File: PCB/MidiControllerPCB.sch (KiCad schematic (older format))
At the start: 148 parts, among them J1 BARREL_JACK, J10 L10_Out, J11 L9_In, J12 L9_Out, J13 4_In, J14 4_Out, J15 3_In, J16 3_Out, J17 2_In, J18 2_Out, J19 1_In, J2 LMain_Out, J20 1_Out, J21 DIN_5, J22 Vol_In, J23 Vol_Out, J24 Tap1, J25 Tap2, J26 ToMainOutL, J27 MainOutL, J28 ToVolInOut, J29 VolInOut, J3 Tap3, J35 Raspberry_Pi_2_3, J4 Tap4, J41 PIC_debug, J44 pi 1=pwr 2=gnd, J5 LEDs / LCD / FootSwitches, J6 Pedal Routes, J7 DIN_5, J8 DIN_5, J9 L10_In, K1 AZ850-x, K10 AZ850-x, K11 AZ850-x, K12 AZ850-x, K13 AZ850-x, K14 AZ850-x, K15 AZ850-x, K16 AZ850-x, K17 AZ850-x, K2 AZ850-x, K3 AZ850-x, K4 AZ850-x, K5 AZ850-x, K6 AZ850-x, K7 AZ850-x, K8 AZ850-x, K9 AZ850-x, Q1 Q_NPN_BEC, Q10 Q_NPN_BEC, Q11 Q_NPN_BEC, Q12 Q_NPN_BEC, Q13 Q_NPN_BEC, Q14 Q_NPN_BEC, Q15 Q_NPN_BEC, Q16 Q_NPN_BEC, Q17 Q_NPN_BEC, Q18 Q_NPN_BEC, Q19 Q_NPN_BEC, Q2 Q_NPN_BEC, Q20 Q_NPN_BEC, Q21 Q_NPN_BEC, Q22 Q_NPN_BEC, Q3 Q_NPN_BEC, Q4 Q_NPN_BEC, Q5 Q_NPN_BEC, Q6 Q_NPN_BEC, Q7 Q_NPN_BEC, Q8 Q_NPN_BEC, Q9 Q_NPN_BEC, U1 MCP23017_ML, U10 PIC18F26K80_IML, U2 MCP23017_ML, U3 MCP23017_ML, U4 MCP23017_ML, U5 CD4050BCN, U6 4N35, U7 7805_PINS, U8 TL072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

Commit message: progress toward schematic being done
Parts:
- removed C15, C17: 10uf, Capacitors_THT:CP_Radial_D4.0mm_P2.00mm, symbol Device:CP1_Small
- removed C16, C18: 0.1uf, Capacitors_THT:C_Axial_L3.8mm_D2.6mm_P7.50mm_Horizontal, symbol Device:C_Small
- removed D1, D10, D11, D12, D13, D14, D15, D17, D2, D20, D22, D3, D4, D5, D6, D7, D8, D9: 1N4001, Diodes_SMD:D_SMA, symbol MidiControllerPCB-rescue:1N4001-LooperPCB-rescue
- removed J1: BARREL_JACK, Connectors:BARREL_JACK, symbol conn:BARREL_JACK
- removed J10: L10_Out, NRJ6HM:NRJ6HM-1-PRE, symbol conn:JACK_TRS_6PINS
- removed J11: L9_In, NRJ6HM:NRJ6HM-1-PRE, symbol conn:JACK_TRS_6PINS
- removed J12: L9_Out, NRJ6HM:NRJ6HM-1-PRE, symbol conn:JACK_TRS_6PINS
- removed J13: 4_In, NRJ6HM:NRJ6HM-1-PRE, symbol conn:JACK_TRS_6PINS
- removed J14: 4_Out, NRJ6HM:NRJ6HM-1-PRE, symbol conn:JACK_TRS_6PINS
- removed J15: 3_In, NRJ6HM:NRJ6HM-1-PRE, symbol conn:JACK_TRS_6PINS
- removed J16: 3_Out, NRJ6HM:NRJ6HM-1-PRE, symbol conn:JACK_TRS_6PINS
- removed J17: 2_In, NRJ6HM:NRJ6HM-1-PRE, symbol conn:JACK_TRS_6PINS
- removed J18: 2_Out, NRJ6HM:NRJ6HM-1-PRE, symbol conn:JACK_TRS_6PINS
- removed J19: 1_In, NRJ6HM:NRJ6HM-1-PRE, symbol conn:JACK_TRS_6PINS
- removed J2: LMain_Out, NRJ6HM:NRJ6HM-1-PRE, symbol conn:JACK_TRS_6PINS
- removed J20: 1_Out, NRJ6HM:NRJ6HM-1-PRE, symbol conn:JACK_TRS_6PINS
- removed J21: DIN_5, stomp:Midi-Connector, symbol conn:DIN_5
- removed J22: Vol_In, NRJ6HM:NRJ6HM-1-PRE, symbol conn:JACK_TRS_6PINS
- removed J23: Vol_Out, NRJ6HM:NRJ6HM-1-PRE, symbol conn:JACK_TRS_6PINS
- removed J26: ToMainOutL, Pin_Headers:Pin_Header_Straight_2x05_Pitch2.54mm, symbol conn:CONN_02X05
- removed J27: MainOutL, Pin_Headers:Pin_Header_Straight_2x05_Pitch2.54mm, symbol conn:CONN_02X05
- removed J28: ToVolInOut, Pin_Headers:Pin_Header_Straight_2x05_Pitch2.54mm, symbol conn:CONN_02X05
- removed J29: VolInOut, Pin_Headers:Pin_Header_Straight_2x05_Pitch2.54mm, symbol conn:CONN_02X05
- removed J44: pi 1=pwr 2=gnd, Pin_Headers:Pin_Header_Straight_1x02_Pitch2.54mm, symbol conn:CONN_01X02
- removed J5: LEDs / LCD / FootSwitches, Pin_Headers:Pin_Header_Straight_2x20_Pitch2.54mm, symbol conn:CONN_02X20
- removed J6: Pedal Routes, Pin_Headers:Pin_Header_Straight_2x20_Pitch2.54mm, symbol conn:CONN_02X20
- removed J9: L10_In, NRJ6HM:NRJ6HM-1-PRE, symbol conn:JACK_TRS_6PINS
- removed K1, K10, K11, K12, K13, K14, K15, K16, K17, K2, K3, K4, K5, K6, K7, K8, K9: AZ850-x, Relays_THT:Relay_DPDT_FRT5, symbol MidiControllerPCB-rescue:AZ850-x-LooperPCB-rescue
- removed Q1, Q10, Q11, Q12, Q13, Q14, Q15, Q16, Q17, Q18, Q19, Q2, Q20, Q21, Q22, Q3, Q4, Q5, Q6, Q7, Q8, Q9: Q_NPN_BEC, TO_SOT_Packages_SMD:SOT-23, symbol Device:Q_NPN_BEC
- removed R1, R10, R11, R12, R13, R14, R2, R3, R30, R34, R4, R45, R5, R6, R7, R8, R9: 100, Resistors_SMD:R_1206_HandSoldering, symbol Device:R_Small
- removed R19, R57, R59, R61, R64: 470, Resistors_SMD:R_1206_HandSoldering, symbol Device:R_Small
- removed R20: 270, Resistors_SMD:R_1206_HandSoldering, symbol Device:R_Small
- removed R43: 1k, Resistors_SMD:R_1206_HandSoldering, symbol Device:R_Small
- removed R58, R60, R62, R65: 4.7k, Resistors_SMD:R_1206_HandSoldering, symbol Device:R_Small
- removed R75, R76, R77, R78, R79: 2.2M, Resistors_SMD:R_0603_HandSoldering, symbol Device:R_Small
- removed TP1: 9V, Pin_Headers:Pin_Header_Straight_1x01_Pitch2.54mm, symbol MidiControllerPCB-rescue:TEST-LooperPCB-rescue
- removed TP2: GND, Pin_Headers:Pin_Header_Straight_1x01_Pitch2.54mm, symbol MidiControllerPCB-rescue:TEST-LooperPCB-rescue
- removed U1, U3, U4: MCP23017_ML, Housings_DFN_QFN:QFN-28-1EP_6x6mm_Pitch0.65mm, symbol Interface_Expansion:MCP23017_ML
- removed U6: 4N35, Housings_DIP:DIP-6_W7.62mm_Socket, symbol 4N35-TTL-Serial-Optoisolator-cache:4N35
- removed U7: 7805_PINS, TO_SOT_Packages_THT:TO-220-3_Vertical, symbol eurocad:7805_PINS
- removed U8, U9: TL072, Housings_SSOP:TSSOP-8_4.4x3mm_Pitch0.65mm, symbol linear:TL072
- added C? (x5): 0.1uf, Capacitors_THT:C_Axial_L3.8mm_D2.6mm_P7.50mm_Horizontal, symbol Device:C_Small
- added C? (x2): 0.01uf, Capacitors_THT:C_Axial_L3.8mm_D2.6mm_P7.50mm_Horizontal, symbol Device:C_Small
- added J?: fan_header, symbol conn:CONN_01X02
- added J?: OLED_Display, symbol conn:CONN_01X07
- added R? (x15): 10k, Resistors_THT:R_Box_L8.4mm_W2.5mm_P5.08mm, symbol Device:R_Small
- added R? (x3): 1k, Resistors_THT:R_Box_L8.4mm_W2.5mm_P5.08mm, symbol Device:R_Small
- added R? (x8): 220, Resistors_SMD:R_1206_HandSoldering, symbol Device:R_Small
- added SW? (x5): SW_SPST, Pin_Headers:Pin_Header_Straight_1x02_Pitch2.54mm, symbol LooperPCB_side-rescue:SW_SPST
- added SW?: RGB_Rotary_Enc_PB, stomp:RGB_ENCODER_8pins, symbol LooperPCB_side-rescue:RGB_Rotary_Enc_PB
- J24: value Tap1 -> TRS_Midi_1
- J25: value Tap2 -> TRS_Midi_2
- J3: value Tap3 -> TRS_Midi_3
- J4: value Tap4 -> TRS_Midi_4
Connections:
- net FootSw6 is gone; now on net FootSw4: U2.25 (GPB0)
- net FootSw8 is gone; now on net FootSw5: U2.27 (GPB2)
- net 1_MIDI_Pin5: now also R18.1, U5.2 (G=A); no longer U5.4 (H=B)
- net 2_MIDI_Pin5: now also R16.1, U5.4 (H=B); no longer U5.2 (G=A)
- net FootSw1: now also C?.1, R?.1
- net FootSw2: now also C?.1, R?.1
- net FootSw3: now also C?.1, R?.1
- net FootSw4: now also C?.1, R?.1; no longer U2.20 (GPA3)
- net FootSw5: now also C?.1, R?.1; no longer U2.21 (GPA4)
- net GND: now also C?.2, C?.2, C?.2, C?.2, C?.2, C?.2, C?.2, J?.1 (P1), J?.2 (P2), R?.2, SW?.1 (A), SW?.1 (A), SW?.1 (A), SW?.1 (A), SW?.1 (A), SW?.2 (C)
- net MIDI_Tx: now also U5.11 (E), U5.14 (F), U5.7 (C), U5.9 (D)
- net RotEncA: now also C?.1, R?.2
- net RotEncB: now also C?.1, R?.1
- net RotEncBlue: now also R?.2
- net RotEncGreen: now also R?.2
- net RotEncPushBttn: now also R?.1, SW?.6 (SW)
- net RotEncRed: now also R?.2
- net VCC: now also J35.2 (5V), J?.1 (P1), R?.1, R?.1, R?.1, R?.1, R?.1, R?.1, R?.2, R?.2, R?.2, R?.2, R?.2, SW?.8 (+)
- net VEE: now also J?.2 (P2)
- net MOSI: now reaches J35.19 ((SPI_MOSI)_GPIO10)
- net MOSI: now also J?.5 (P5)
- net Reset: now reaches J35.22 (GPIO25_(GEN6))
- net Reset: now also J?.7 (P7)
- net SCLK: now reaches J35.23 ((SPI_SCLK)_GPIO11)
- net SCLK: now also J?.4 (P4)
- net ChipSelectEnable: now reaches J35.26 ((~SPI_CE1~)_GPIO7)
- net ChipSelectEnable: now also J?.6 (P6)
- net DataCommand: now reaches J35.32 (GPIO12)
- net DataCommand: now also J?.3 (P3)
- net at J3.2 (T): now also R?.2
- net at J4.2 (T): now also R?.2
- net at J24.2 (T): now also R?.2
- net at J25.2 (T): now also R?.2
- net 2_TRS_MIDI_Tip: now reaches U5.10 (J=D)
- net 2_TRS_MIDI_Tip: now also R?.1
- net 3_TRS_MIDI_Tip: now reaches U5.12 (K=E)
- net 3_TRS_MIDI_Tip: now also R?.1
- net 4_TRS_MIDI_Tip: now reaches U5.15 (L=F)
- net 4_TRS_MIDI_Tip: now also R?.1
- net 1_TRS_MIDI_Tip: now reaches U5.6 (I=C)
- net 1_TRS_MIDI_Tip: now also R?.1
- net at J3.3 (R): now also R?.2
- net at J4.3 (R): now also R?.2
- net at J24.3 (R): now also R?.2
- net at J25.3 (R): now also R?.2
- net FootSw10: no longer names the net of U2.1 (GPB4)
- net FootSw7: no longer names the net of U2.26 (GPB1)
- net FootSw9: no longer names the net of U2.28 (GPB3)
- net MIDI_Rx: no longer names the net of U10.15 (CANRX/RX1/CCP4/RC7)
- new net: R?.1, R?.2, SW?.2 (B) (x5)
- new net: R?.1, R?.2, SW?.1 (A)
- new net: R?.1, SW?.4 (R)
- new net: R?.1, SW?.5 (G)
- new net: R?.1, SW?.7 (BL)
- new net: R?.2, R?.2, SW?.3 (B)
- no-connect marks 172 -> 64
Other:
- moved on the sheet: C13, C14, J24, J25, J3, J35, J4, J41, J7, J8, R15, R16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

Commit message: schematic: nothing todo list: modify notes
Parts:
- C1, C2, C3, C4, C5, C6, C7: renamed from C?; footprint Capacitors_THT:C_Axial_L3.8mm_D2.6mm_P7.50mm_Horizontal -> Capacitors_SMD:C_1206_HandSoldering
- C13, C14: footprint Capacitors_THT:C_Axial_L3.8mm_D2.6mm_P7.50mm_Horizontal -> Capacitors_SMD:C_1206_HandSoldering
- J1: renamed from J?; footprint (none) -> Pin_Headers:Pin_Header_Straight_1x07_Pitch1.00mm
- J2: renamed from J?; footprint (none) -> Pin_Headers:Pin_Header_Straight_1x02_Pitch2.54mm
- R10, R11, R12, R13, R14, R19, R20, R21, R22, R23, R24, R25, R26, R27, R28, R29, R30, R9: renamed from R?; footprint Resistors_THT:R_Box_L8.4mm_W2.5mm_P5.08mm -> Resistors_SMD:R_1206_HandSoldering
- SW1, SW2, SW3, SW4, SW5: renamed from SW?; symbol LooperPCB_side-rescue:SW_SPST -> MidiControllerPCB-rescue:SW_SPST-LooperPCB_side-rescue
- SW6: renamed from SW?; footprint stomp:RGB_ENCODER_8pins -> Pin_Headers:Pin_Header_Straight_2x04_Pitch2.54mm; symbol LooperPCB_side-rescue:RGB_Rotary_Enc_PB -> MidiControllerPCB-rescue:RGB_Rotary_Enc_PB-LooperPCB_side-rescue
- gave numbers to parts that had none: 8
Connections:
- no-connect marks 64 -> 65

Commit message: board finished. need fab files
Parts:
- J1: footprint Pin_Headers:Pin_Header_Straight_1x07_Pitch1.00mm -> Pin_Headers:Pin_Header_Straight_1x07_Pitch1.27mm
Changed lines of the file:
@@
 F 0 "J1" H 18350 10050 50  0000 C CNN
 F 1 "OLED_Display" V 18500 10500 50  0000 C CNN
-F 2 "Pin_Headers:Pin_Header_Straight_1x07_Pitch1.00mm" H 18350 10500 50  0001 C CNN
+F 2 "Pin_Headers:Pin_Header_Straight_1x07_Pitch1.27mm" H 18350 10500 50  0001 C CNN
 F 3 "" H 18350 10500 50  0001 C CNN
 	1    18350 10500

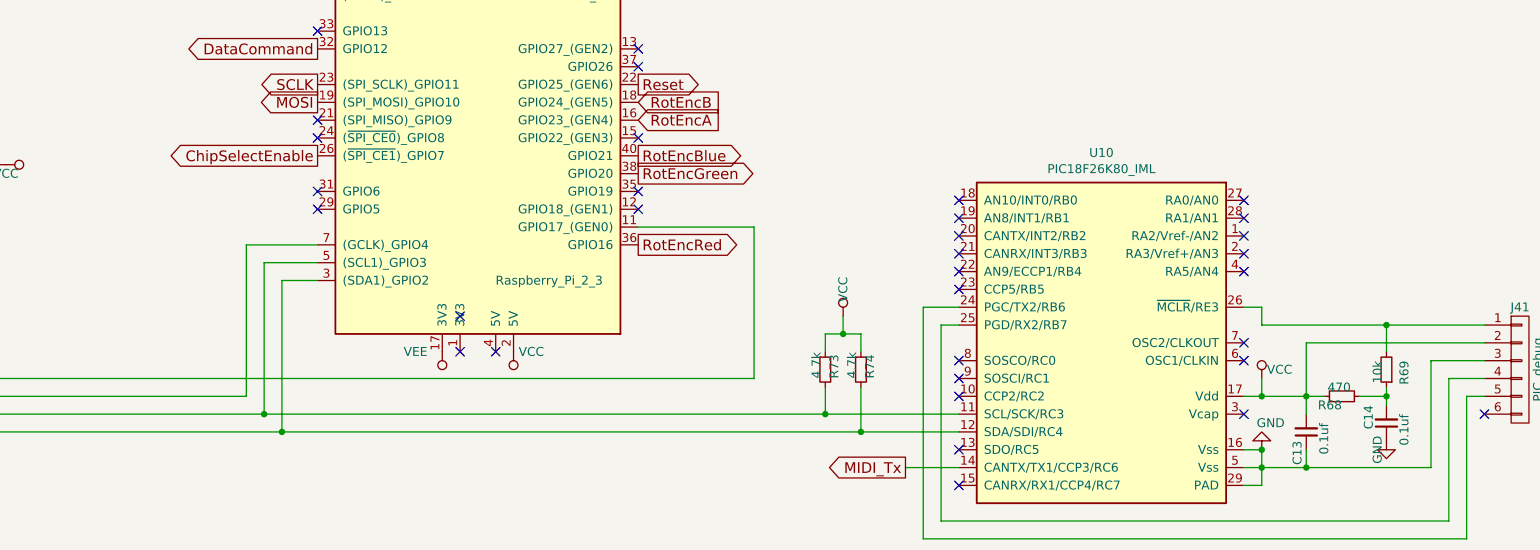
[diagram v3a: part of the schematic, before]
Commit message: modify pcb
1. move the SPI chip enable wire that controls the OLED from rpi CE1 to CE0
2. swap r68 and r69 as they are in the wrong positions... opps
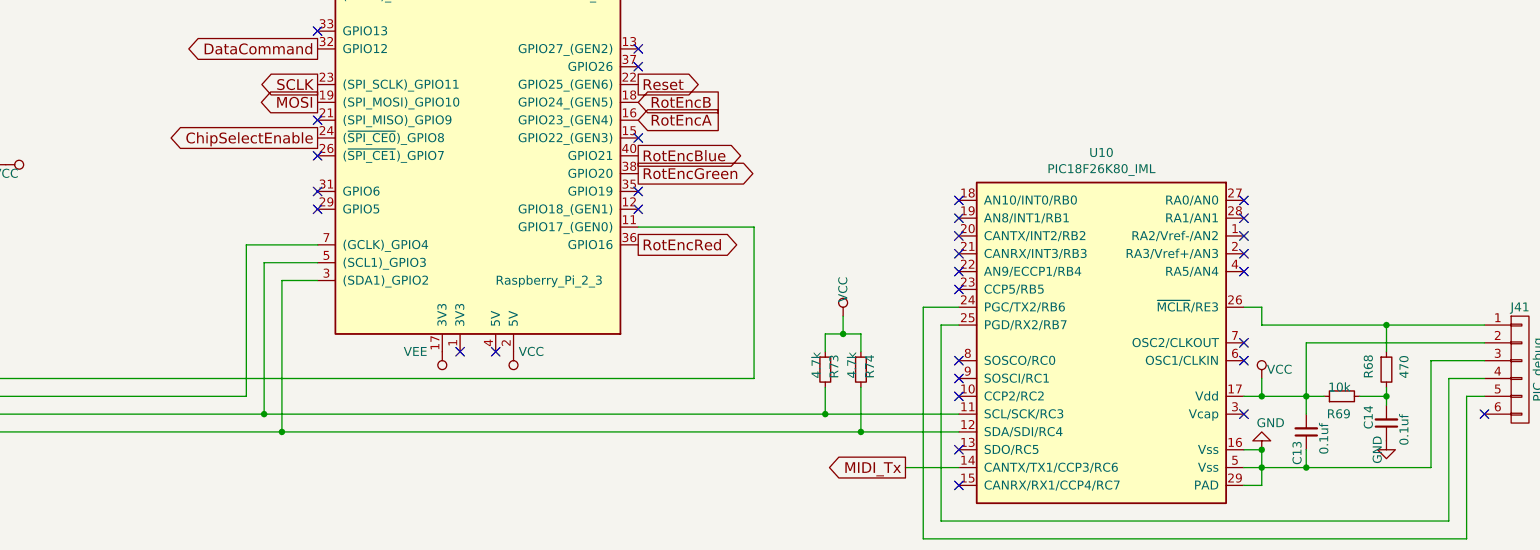
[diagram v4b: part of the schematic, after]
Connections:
- net ChipSelectEnable: now also J35.24 ((~SPI_CE0~)_GPIO8); no longer J35.26 ((~SPI_CE1~)_GPIO7)
- net VCC: now also R69.1; no longer R68.1
- net at C14.2, R68.2: now also R69.2; no longer R69.1
- net at J41.1 (P1), U10.26 (~MCLR~/RE3): now also R68.1; no longer R69.2
- no-connect marks 65 -> 64
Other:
- moved on the sheet: R68, R69
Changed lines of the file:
@@
 L Device:R_Small R68
 U 1 1 5992FFE6
+P 22750 8550
+F 0 "R68" V 22650 8500 50  0000 L CNN
+F 1 "470" V 22850 8500 50  0000 L CNN
+F 2 "Resistors_SMD:R_1206_HandSoldering" H 22750 8550 50  0001 C CNN
+F 3 "" H 22750 8550 50  0001 C CNN
+	1    22750 8550
+	1    0    0    -1
+$EndComp
+$Comp
+L Device:R_Small R69
+U 1 1 59931B2A
 P 22500 8700
-F 0 "R68" V 22450 8700 50  0000 L CNN
-F 1 "470" V 22550 8650 50  0000 L CNN
+F 0 "R69" V 22400 8650 50  0000 L CNN
+F 1 "10k" V 22550 8650 50  0000 L CNN
 F 2 "Resistors_SMD:R_1206_HandSoldering" H 22500 8700 50  0001 C CNN
 F 3 "" H 22500 8700 50  0001 C CNN
 	1    22500 8700
 	0    -1   -1   0
-$EndComp
-$Comp
-L Device:R_Small R69
-U 1 1 59931B2A
-P 22750 8550
-F 0 "R69" V 22650 8500 50  0000 L CNN
-F 1 "10k" V 22800 8500 50  0000 L CNN
-F 2 "Resistors_SMD:R_1206_HandSoldering" H 22750 8550 50  0001 C CNN
-F 3 "" H 22750 8550 50  0001 C CNN
-	1    22750 8550
-	-1   0    0    1
 $EndComp
 $Comp
@@
 NoConn ~ 17750 8450
 NoConn ~ 23300 8800
-NoConn ~ 16750 7250
 NoConn ~ 16750 7150
 NoConn ~ 16750 6450
@@
 Text GLabel 16750 7050 0    60   Output ~ 0
 MOSI
-Text GLabel 16750 7350 0    60   Output ~ 0
+Text GLabel 16750 7250 0    60   Output ~ 0
 ChipSelectEnable
 Text GLabel 18550 6950 2    60   Output ~ 0
 Reset
 NoConn ~ 16750 7650
-NoConn ~ 17550 8250
+NoConn ~ 16750 7350
 $EndSCHEMATC
